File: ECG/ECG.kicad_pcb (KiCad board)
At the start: 4 copper layers, 81.3 x 109.2 mm, 80 parts, among them J1 Conn_01x03, J2 Conn_01x03, J3 Conn_01x15, J4 Conn_01x15, J5 Conn_01x02, J6 Conn_01x02, J7 Conn_01x02, J8 Conn_01x02, Q1 DMG2301L, Q2 T2N7002AK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

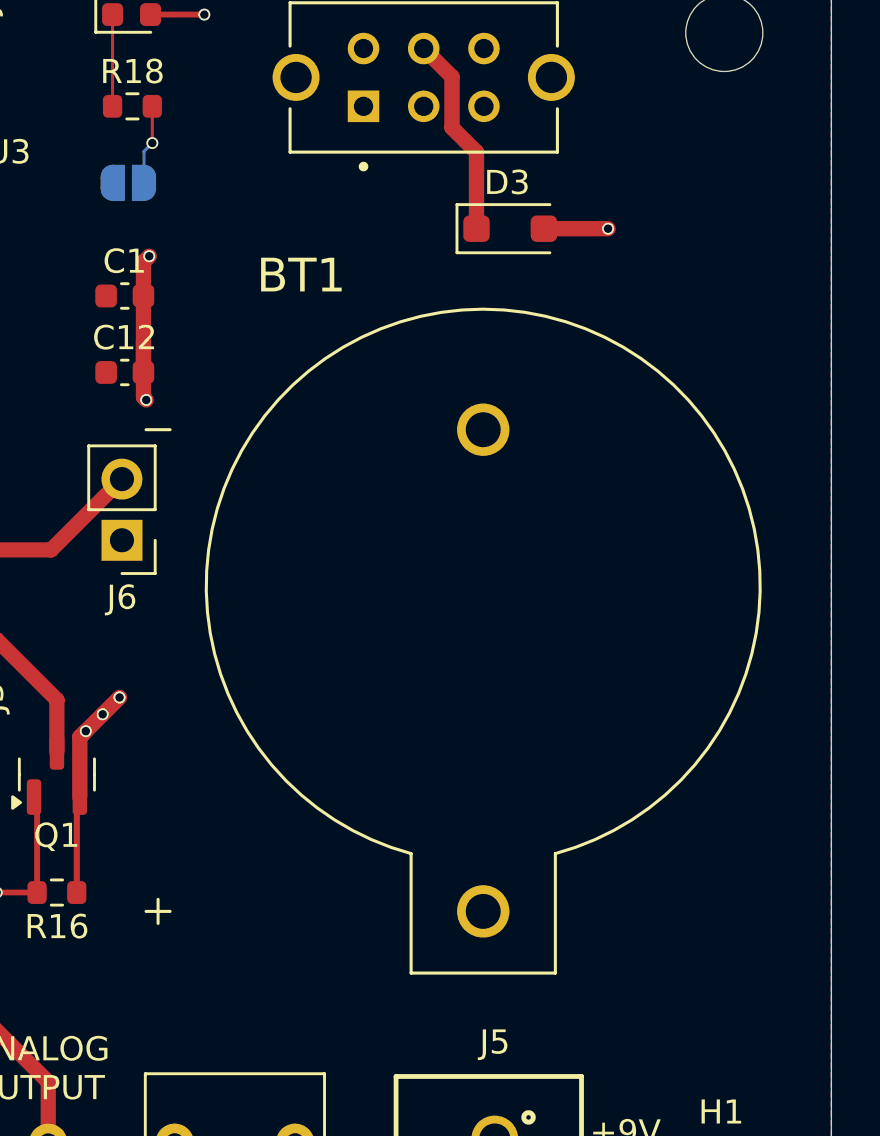
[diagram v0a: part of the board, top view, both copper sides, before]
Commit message: Change coin cell holder to one the is dummy "proof"
Close #14
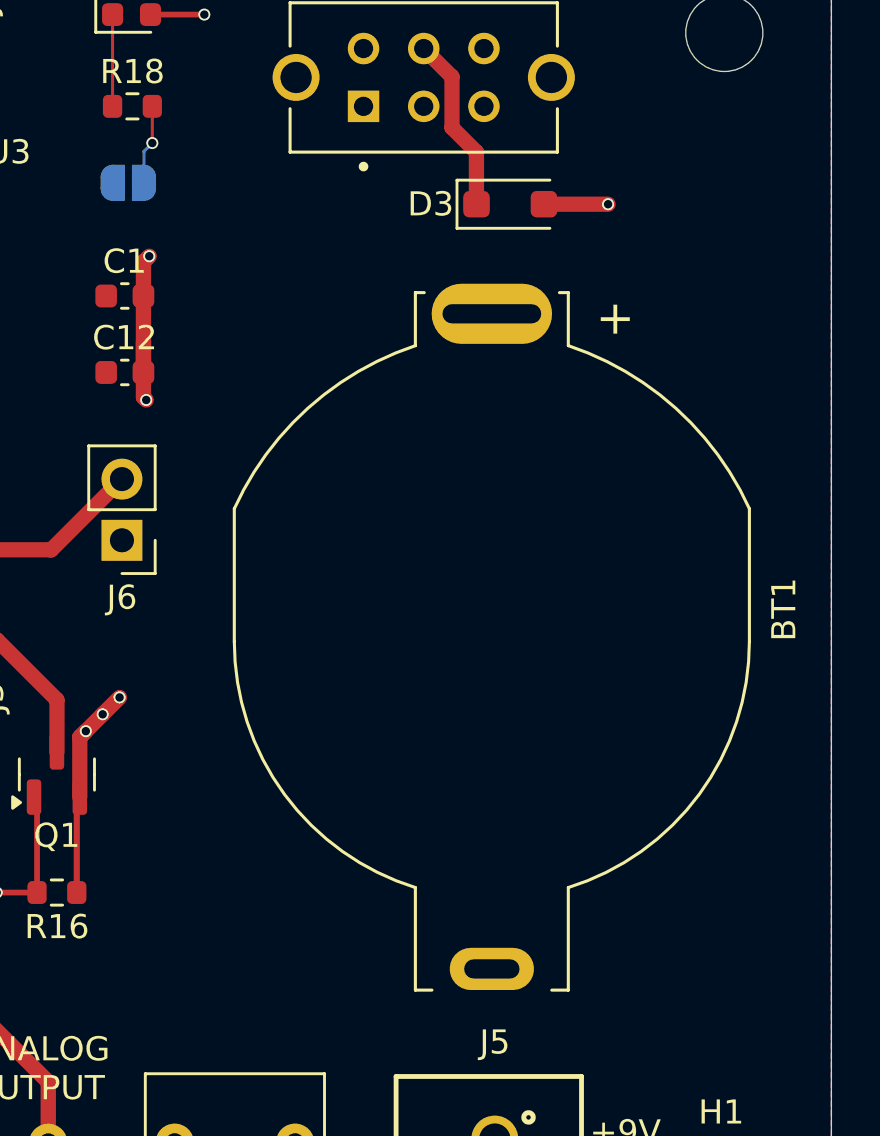
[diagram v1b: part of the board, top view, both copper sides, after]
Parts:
- BT1: value BS-3 -> BC2032-E2; footprint ECG_Footprints:BAT_BS-3 -> ECG_Footprints:MPD_BC2032-E2
- moved BT1 2.32 mm to (159.3, 54.5), turned to -90 degrees
- moved D3 1.02 mm to (160.0, 36.3)
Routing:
- net Net-(D3-A): track 45.4 -> 46.4 mm
- net Net-(D3-K): track 8.39 -> 7.37 mm

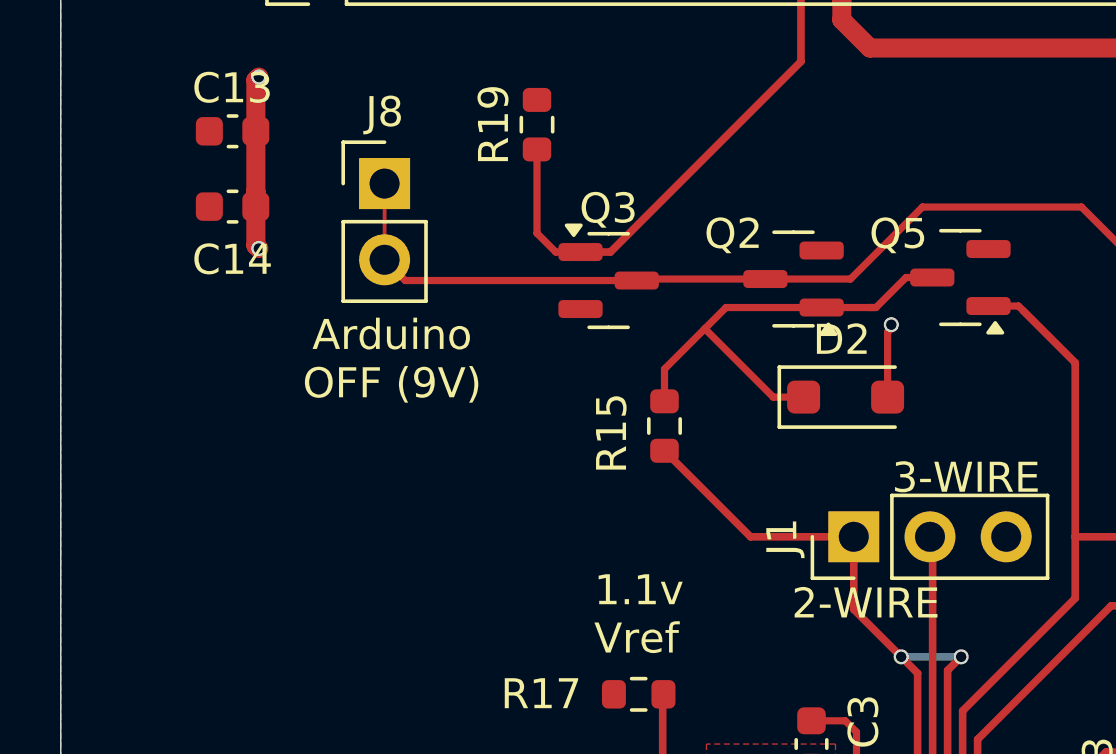
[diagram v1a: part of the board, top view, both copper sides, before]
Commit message: Add control of LeadsOn from AD3
Close #16
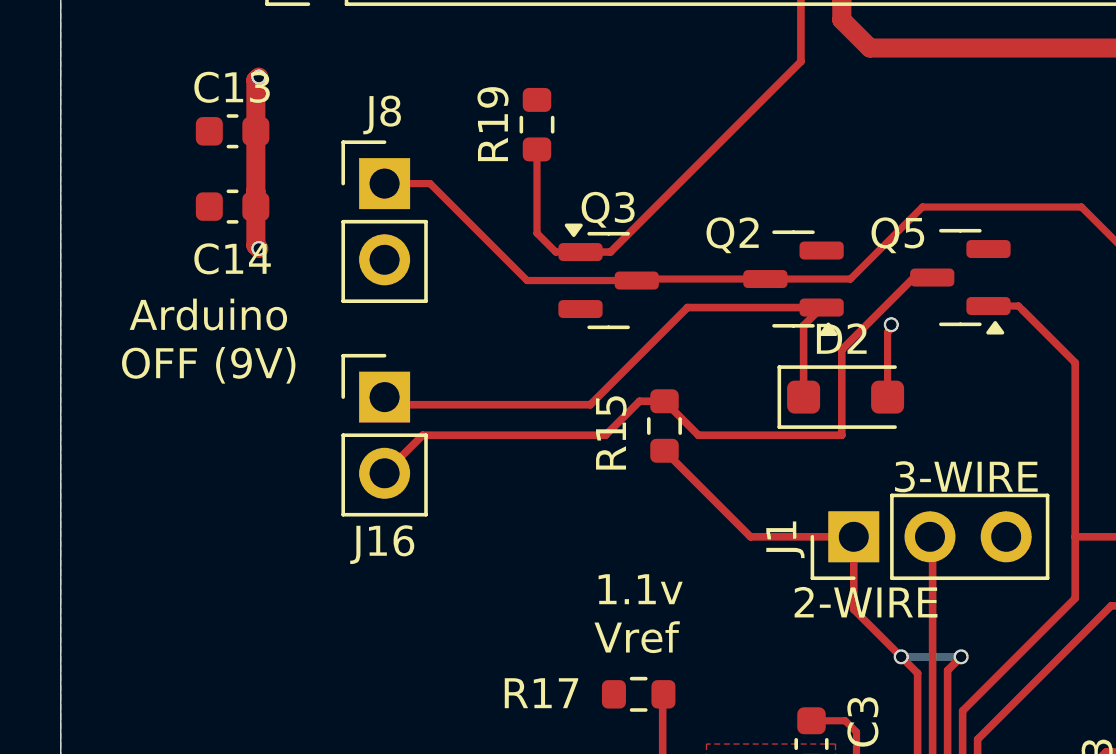
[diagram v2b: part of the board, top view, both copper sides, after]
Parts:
- added J16: Conn_01x02, Connector_PinHeader_2.54mm:PinHeader_1x02_P2.54mm_Vertical, F.Cu at (102.9, 72.1)
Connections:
- D2 pad 1: /LEADS_ON -> Net-(D2-K)
- J8 pad 2: /PWR_OFF_HV -> GND
- Q2 pad 1: /LEADS_ON -> Net-(D2-K)
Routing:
- net Net-(D2-K): track 0.00 -> 19.8 mm
- net /LEADS_ON: track 15.7 -> 23.6 mm
- net /PWR_OFF_HV: track 46.9 -> 45.4 mm

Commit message: Work on AD3 connection stuff
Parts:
- removed J16: Conn_01x02, Connector_PinHeader_2.54mm:PinHeader_1x02_P2.54mm_Vertical
- J8: value Conn_01x02 -> Conn_02x05_Odd_Even; footprint Connector_PinHeader_2.54mm:PinHeader_1x02_P2.54mm_Vertical -> Connector_PinSocket_2.54mm:PinSocket_2x05_P2.54mm_Vertical
- JP3: value SolderJumper_2_Open -> SolderJumper_2_Bridged; footprint Jumper:SolderJumper-2_P1.3mm_Open_RoundedPad1.0x1.5mm -> Jumper:SolderJumper-2_P1.3mm_Bridged_RoundedPad1.0x1.5mm
- moved C14 23.2 mm to (120.9, 63.8), turned to 90 degrees
- moved C13 20.6 mm to (118.4, 63.8), turned to 90 degrees
- moved J8 9.75 mm to (101.3, 74.6), turned to 180 degrees
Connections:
- J8 pad 1: /PWR_OFF_HV -> /LEADS_ON
- J8 pad 2: GND -> Net-(D2-K)
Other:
- board text removed: "Arduino OFF (9V)"

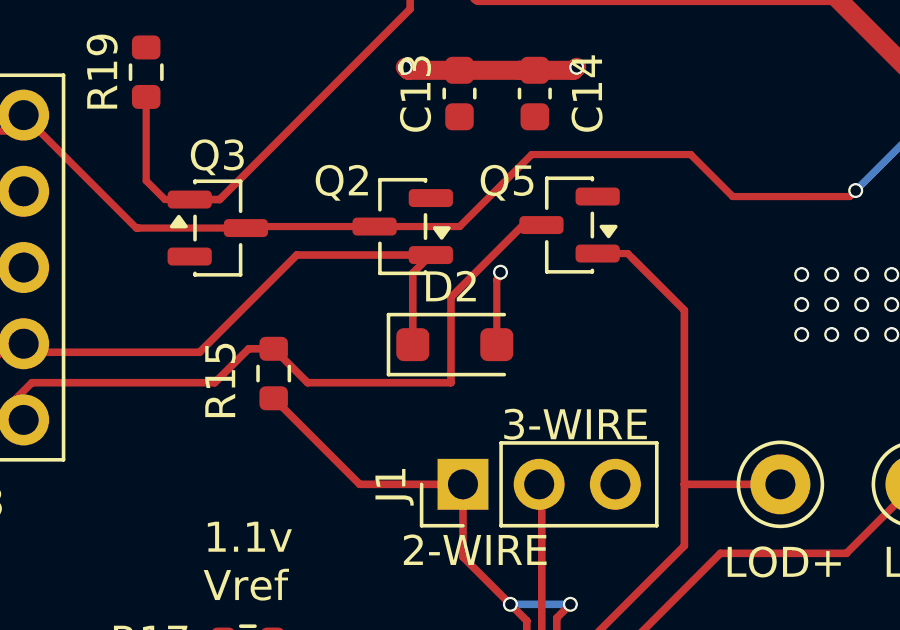
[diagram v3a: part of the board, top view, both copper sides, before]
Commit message: Manually merge commit d0bb662.
Low leakage schottky for protection.
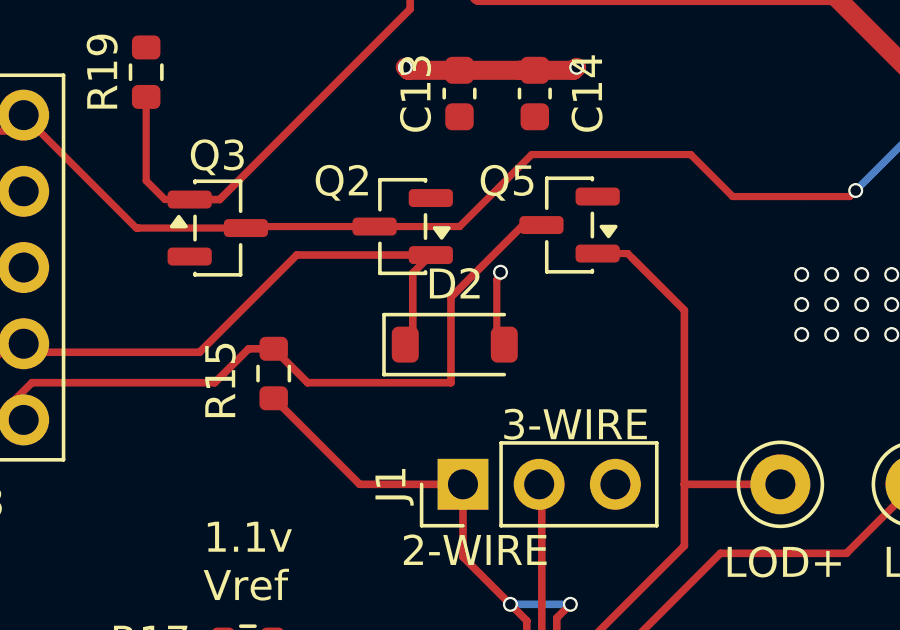
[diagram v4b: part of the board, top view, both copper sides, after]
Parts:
- D2: footprint Diode_SMD:D_SOD-123F -> Diode_SMD:D_SOD-123
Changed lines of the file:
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@@
 		)
 	)
-	(footprint "Diode_SMD:D_SOD-123F"
+	(footprint "Diode_SMD:D_SOD-123"
 		(layer "F.Cu")
 		(at 118.237 72.136)
-		(descr "D_SOD-123F")
-		(tags "D_SOD-123F")
+		(descr "SOD-123")
+		(tags "SOD-123")
 		(property "Reference" "D2"
-			(at -0.127 -1.905 0)
+			(at 0 -2 0)
 			(layer "F.SilkS")
 			(effects
@@
 			)
 		)
-		(property "DigikeyPN" "1727-3853-1-ND"
+		(property "DigikeyPN" "SM5817PL-TPMSCT-ND"
 			(at 0 0 0)
 			(unlocked yes)
@@
 		(attr smd)
 		(fp_line
-			(start -2.21 -1)
-			(end -2.21 1)
+			(start -2.36 -1)
+			(end -2.36 1)
 			(stroke
 				(width 0.12)
@@
 		)
 		(fp_line
-			(start -2.21 -1)
+			(start -2.36 -1)
 			(end 1.65 -1)
 			(stroke
@@
 		)
 		(fp_line
-			(start -2.21 1)
+			(start -2.36 1)
 			(end 1.65 1)
 			(stroke
@@
 		)
 		(fp_line
-			(start -2.2 -1.15)
-			(end -2.2 1.15)
-			(stroke
-				(width 0.05)
-				(type solid)
-			)
-			(layer "F.CrtYd")
-		)
-		(fp_line
-			(start -2.2 -1.15)
-			(end 2.2 -1.15)
-			(stroke
-				(width 0.05)
-				(type solid)
-			)
-			(layer "F.CrtYd")
-		)
-		(fp_line
-			(start 2.2 -1.15)
-			(end 2.2 1.15)
-			(stroke
-				(width 0.05)
-				(type solid)
-			)
-			(layer "F.CrtYd")
-		)
-		(fp_line
-			(start 2.2 1.15)
-			(end -2.2 1.15)
+			(start -2.35 -1.15)
+			(end -2.35 1.15)
+			(stroke
+				(width 0.05)
+				(type solid)
+			)
+			(layer "F.CrtYd")
+		)
+		(fp_line
+			(start -2.35 -1.15)
+			(end 2.35 -1.15)
+			(stroke
+				(width 0.05)
+				(type solid)
+			)
+			(layer "F.CrtYd")
+		)
+		(fp_line
+			(start 2.35 -1.15)
+			(end 2.35 1.15)
+			(stroke
+				(width 0.05)
+				(type solid)
+			)
+			(layer "F.CrtYd")
+		)
+		(fp_line
+			(start 2.35 1.15)
+			(end -2.35 1.15)
 			(stroke
 				(width 0.05)
@@
 		)
 		(fp_text user "${REFERENCE}"
-			(at 3.556 0.127 0)
+			(at 0 -2 0)
 			(layer "F.Fab")
 			(effects
@@
 		)
 		(pad "1" smd roundrect
-			(at -1.4 0)
-			(size 1.1 1.1)
+			(at -1.65 0)
+			(size 0.9 1.2)
 			(layers "F.Cu" "F.Mask" "F.Paste")
-			(roundrect_rratio 0.2272727273)
+			(roundrect_rratio 0.25)
 			(net 66 "Net-(D2-K)")
 			(pinfunction "K")
@@
 		)
 		(pad "2" smd roundrect
-			(at 1.4 0)
-			(size 1.1 1.1)
+			(at 1.65 0)
+			(size 0.9 1.2)
 			(layers "F.Cu" "F.Mask" "F.Paste")
-			(roundrect_rratio 0.2272727273)
+			(roundrect_rratio 0.25)
 			(net 63 "/LEADS_ON_PROT")
 			(pinfunction "A")
@@
 		)
 		(embedded_fonts no)
-		(model "${KICAD9_3DMODEL_DIR}/Diode_SMD.3dshapes/D_SOD-123F.step"
+		(model "${KICAD9_3DMODEL_DIR}/Diode_SMD.3dshapes/D_SOD-123.step"
 			(offset
 				(xyz 0 0 0)

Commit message: cleanup layout
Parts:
- D3: footprint Diode_SMD:D_SOD-123F -> Diode_SMD:D_SOD-123
- moved J8 2.40 mm to (100.4, 72.4)
- moved D3 0.18 mm to (160.2, 36.3)
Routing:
- net /OUT: track 26.2 -> 62.6 mm, vias 0 -> 1
- net /LEADS_ON: track 23.6 -> 27.7 mm
- net Net-(D2-K): track 19.8 -> 23.6 mm
- net Net-(J8-Pin_4): track 0.00 -> 2.54 mm
- net GND: vias 99 -> 107

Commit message: Cleanup layout.
Close #17
Close #15
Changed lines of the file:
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@@
 		(tags "C Rect series Radial pin pitch 5.00mm length 7.2mm width 5.5mm Capacitor")
 		(property "Reference" "C2"
-			(at 2.5 -4 90)
+			(at 7.130999 0.137999 180)
 			(layer "F.SilkS")
 			(effects
@@
 			(at 2.332799 -1.792201 90)
 			(layer "F.SilkS")
+			(hide yes)
 			(effects
 				(font
@@
 		(tags "C Rect series Radial pin pitch 5.00mm length 7.2mm width 5.5mm Capacitor")
 		(property "Reference" "C6"
-			(at 2.5 -4 90)
+			(at 7.202999 -0.104001 180)
 			(layer "F.SilkS")
 			(effects
@@
 		(tags "capacitor")
 		(property "Reference" "C16"
-			(at 0 -1.43 0)
+			(at 0 1.524 0)
 			(layer "F.SilkS")
-			(hide yes)
 			(effects
 				(font
@@
 		(tags "SOD-123")
 		(property "Reference" "D2"
-			(at 0 -2 0)
+			(at 3.937 0 0)
 			(layer "F.SilkS")
 			(effects
@@
 		(tags "C Rect series Radial pin pitch 5.00mm length 7.2mm width 5.5mm Capacitor")
 		(property "Reference" "C22"
-			(at 2.5 -4 90)
+			(at 7.130999 0.533999 180)
 			(layer "F.SilkS")
 			(effects
@@
 		(tags "SOD-123")
 		(property "Reference" "D3"
-			(at 0 -2 0)
+			(at -3.9888 0 0)
 			(layer "F.SilkS")
 			(effects
@@
 		(tags "Resistor Axial_DIN0207 series Axial Vertical pin pitch 2.54mm 0.25W = 1/4W length 6.3mm diameter 2.5mm")
 		(property "Reference" "R11"
-			(at 2.459799 -1.449801 90)
+			(at -2.413 1.526001 180)
 			(layer "F.SilkS")
 			(effects
@@
 		(tags "C Rect series Radial pin pitch 5.00mm length 7.2mm width 5.5mm Capacitor")
 		(property "Reference" "C21"
-			(at 2.5 -4 90)
+			(at 7.202999 0.015999 180)
 			(layer "F.SilkS")
 			(effects
@@
 		(tags "resistor")
 		(property "Reference" "R12"
-			(at 0 -1.43 90)
+			(at 3.130999 -0.127 90)
 			(layer "F.SilkS")
 			(effects
@@
 		)
 		(fp_text user "*"
-			(at 1 -3.0954 180)
-			(unlocked yes)
-			(layer "F.SilkS")
-			(effects
-				(font
-					(size 1 1)
-					(thickness 0.15)
-				)
-			)
-		)
-		(fp_text user "*"
-			(at 1 -3.0954 180)
+			(at 0.987602 -3.639 180)
 			(layer "F.SilkS")
 			(effects
@@
 	)
 	(gr_text "3-WIRE"
-		(at 135.255 100.965 0)
+		(at 132.842 101.346 0)
 		(layer "F.SilkS")
 		(effects
@@
 	)
 	(gr_text "3-WIRE\n"
-		(at 119.780001 75.412999 0)
+		(at 119.780001 75.184 0)
 		(layer "F.SilkS")
 		(effects
@@
 			)
 		)
+	)
+	(zone
+		(net 0)
+		(net_name "")
+		(layer "F.Cu")
+		(hatch edge 0.5)
+		(connect_pads
+			(clearance 0)
+		)
+		(min_thickness 0.25)
+		(filled_areas_thickness no)
+		(keepout
+			(tracks allowed)
+			(vias allowed)
+			(pads allowed)
+			(copperpour not_allowed)
+			(footprints allowed)
+		)
+		(placement
+			(enabled no)
+			(sheetname "")
+		)
+		(fill
+			(thermal_gap 0.5)
+			(thermal_bridge_width 0.5)
+		)
+		(polygon
+			(pts
+				(xy 119.126 85.598) (xy 120.142 85.598) (xy 120.142 86.614) (xy 119.126 86.614)
+			)
+		)

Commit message: update qr code
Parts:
- G***: footprint ECG_Footprints:ECG_V1.0b -> ECG_Footprints:ECG_V1.0c

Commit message: work on manufacturing
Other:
- board text added: "AD8232 ECG Demo Board Rev 1.0c Odame/Truex/Barry Copyright 2025"
- board text removed: "AD8232 ECG Demo Board Rev 1.0b Odame/Truex/Barry Copyright 2025"
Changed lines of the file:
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@@
 			(plotframeref no)
 			(mode 1)
-			(useauxorigin no)
+			(useauxorigin yes)
 			(hpglpennumber 1)
 			(hpglpenspeed 20)
@@
 			(drillshape 0)
 			(scaleselection 1)
-			(outputdirectory "Gerber/V1.0b/")
+			(outputdirectory "Gerber/V1.0c/")
 		)
 	)
@@
 		(sheetname "/")
 		(sheetfile "ECG.kicad_sch")
-		(attr through_hole)
+		(attr through_hole dnp)
 		(fp_circle
 			(center 0 0)
@@
 		(sheetname "/")
 		(sheetfile "ECG.kicad_sch")
-		(attr through_hole)
+		(attr through_hole dnp)
 		(fp_circle
 			(center 0 0)
@@
 		(sheetname "/")
 		(sheetfile "ECG.kicad_sch")
-		(attr through_hole)
+		(attr through_hole dnp)
 		(fp_circle
 			(center 0 0)
@@
 		(sheetname "/")
 		(sheetfile "ECG.kicad_sch")
-		(attr through_hole)
+		(attr through_hole dnp)
 		(fp_circle
 			(center 0 0)
@@
 		(sheetname "/")
 		(sheetfile "ECG.kicad_sch")
-		(attr through_hole)
+		(attr through_hole dnp)
 		(fp_circle
 			(center 0 0)
@@
 		(sheetname "/")
 		(sheetfile "ECG.kicad_sch")
-		(attr through_hole)
+		(attr through_hole dnp)
 		(fp_circle
 			(center 0 0)
@@
 		(sheetname "/")
 		(sheetfile "ECG.kicad_sch")
-		(attr through_hole)
+		(attr through_hole dnp)
 		(fp_circle
 			(center 0 0)
@@
 		(sheetname "/")
 		(sheetfile "ECG.kicad_sch")
-		(attr through_hole)
+		(attr through_hole dnp)
 		(fp_circle
 			(center 0 0)
@@
 		)
 	)
-	(gr_text "AD8232 ECG Demo Board\nRev 1.0b \nOdame/Truex/Barry\nCopyright 2025\n"
+	(gr_text "AD8232 ECG Demo Board\nRev 1.0c \nOdame/Truex/Barry\nCopyright 2025\n"
 		(at 116.713 45.974 0)
 		(layer "F.SilkS")
